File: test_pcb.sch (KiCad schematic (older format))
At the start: 25 parts, among them J1 Conn_01x04_Male, J11 Conn_01x20_Female, J8 Conn_01x20_Female, SW1 on/off, SW2 on/off

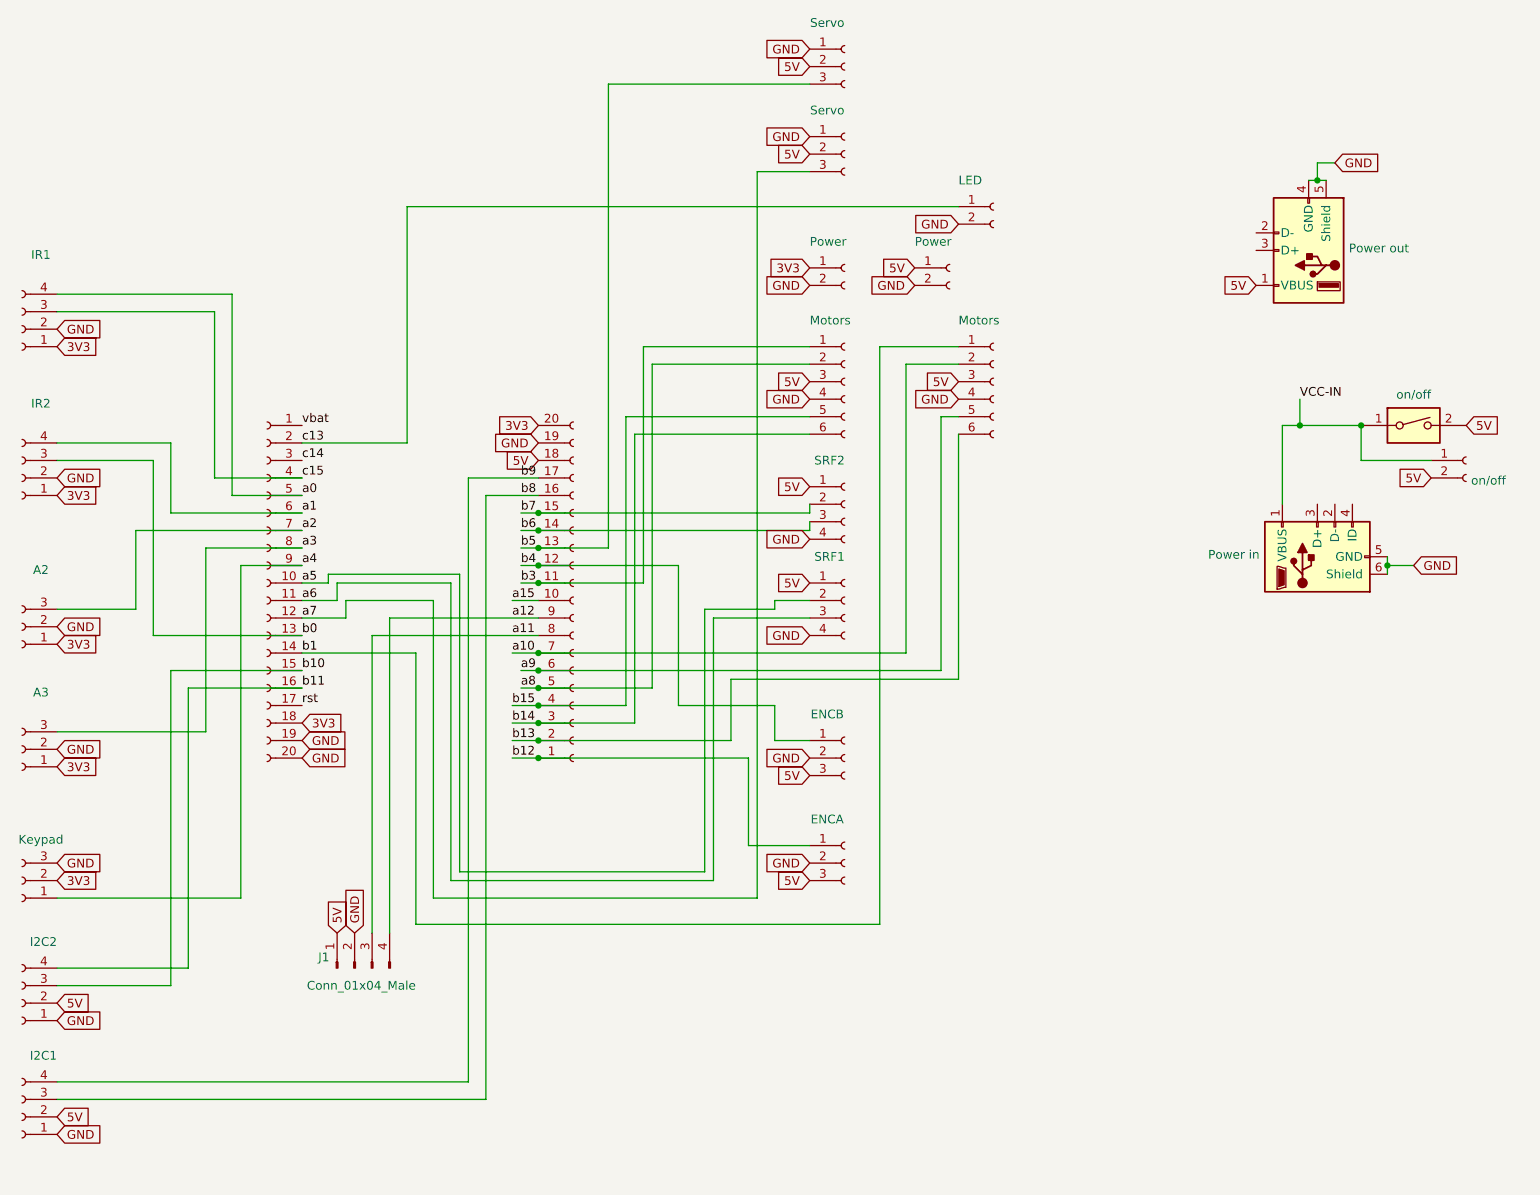
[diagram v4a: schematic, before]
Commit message: routing and shaping, added bom draft
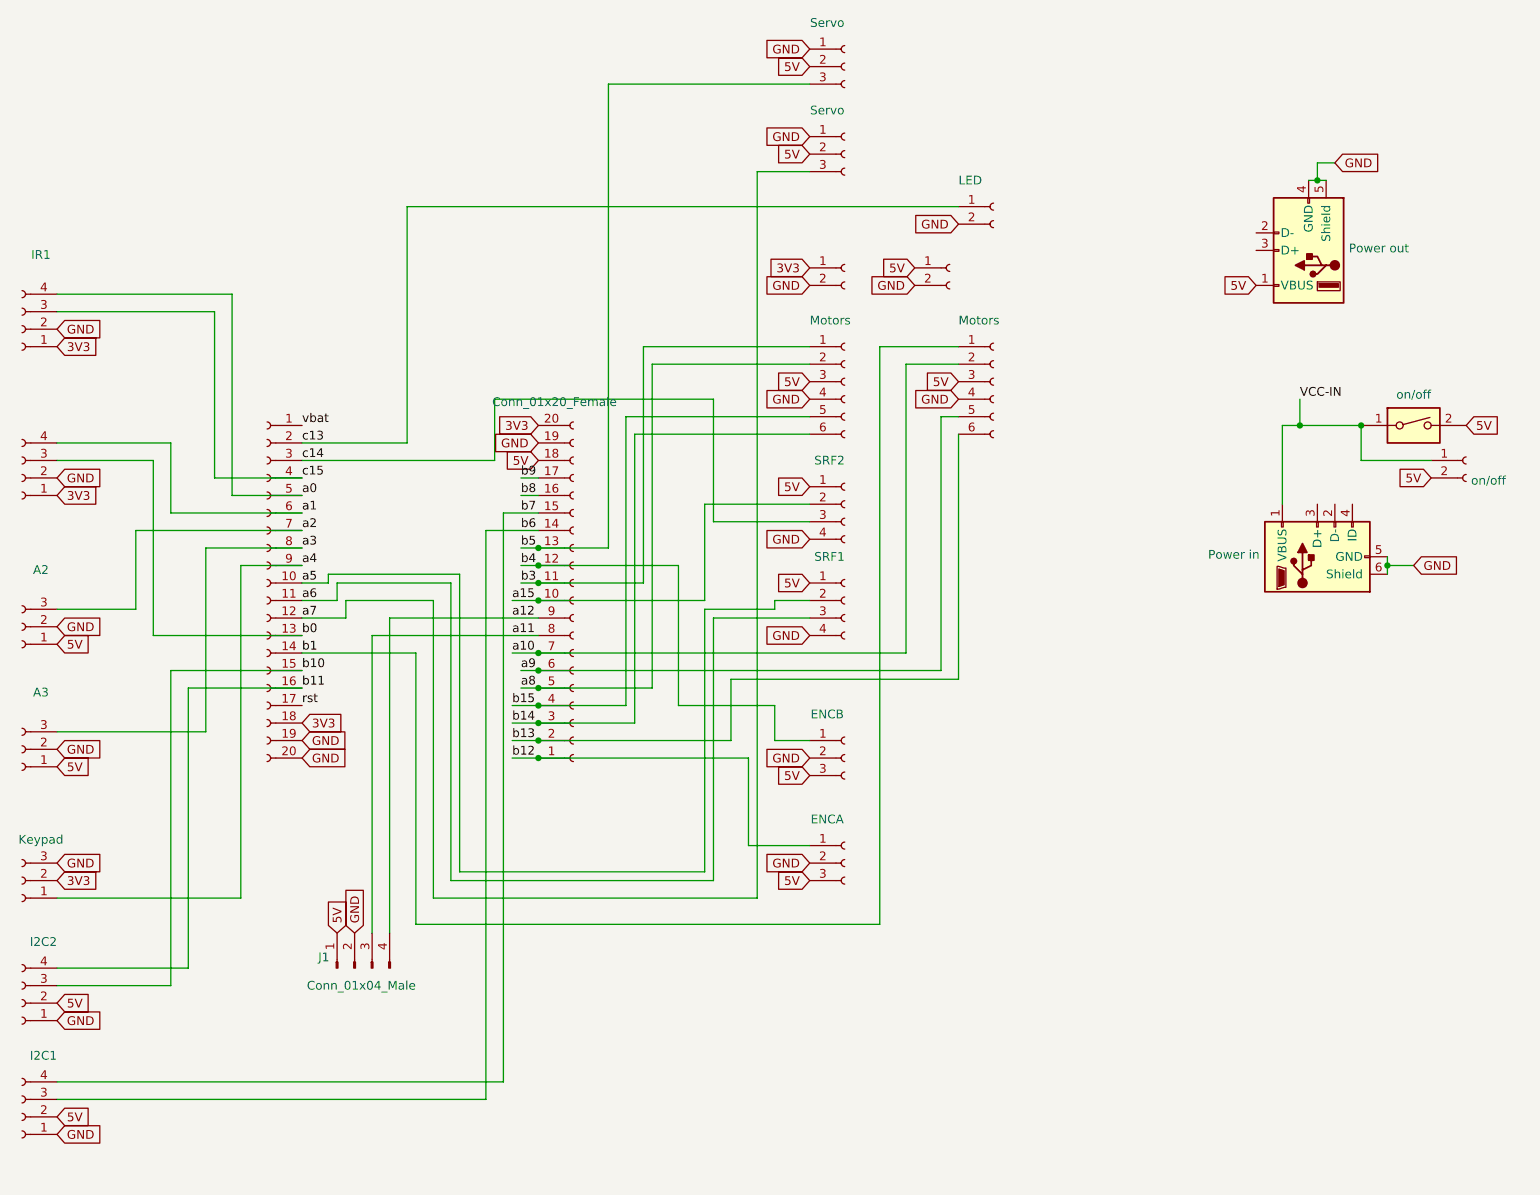
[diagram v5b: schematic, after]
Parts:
- A2: value (A2 GND 3V3) -> A2
- A3: value (A3 GND 3V3) -> A3
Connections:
- net 3V3: no longer A2.1 (Pin_1), A3.1 (Pin_1)
- net 5V: now also A2.1 (Pin_1), A3.1 (Pin_1)
- net a15: now also SRF2.2 (Pin_2)
- net b6: now also I2C1.3 (Pin_3); no longer SRF2.3 (Pin_3)
- net b7: now also I2C1.4 (Pin_4); no longer SRF2.2 (Pin_2)
- net b8: no longer I2C1.3 (Pin_3)
- net b9: no longer I2C1.4 (Pin_4)
- net c14: now also SRF2.3 (Pin_3)
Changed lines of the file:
@@
 P 4100 4300
 F 0 "J11" H 3992 3075 50  0001 C CNN
-F 1 "Conn_01x20_Female" H 3992 3166 50  0001 C CNN
+F 1 "Conn_01x20_Female" H 3992 3166 50  0000 C CNN
 F 2 "Connector_PinSocket_2.54mm:PinSocket_1x20_P2.54mm_Vertical" H 4100 4300 50  0001 C CNN
 F 3 "~" H 4100 4300 50  0001 C CNN
@@
 $EndComp
 $Comp
-L Connector:Conn_01x03_Female A3
-U 1 1 5F73020F
-P 950 5150
-F 0 "A3" H 842 4825 50  0000 C CNN
-F 1 "(A3 GND 3V3)" H 842 4916 50  0001 C CNN
-F 2 "Connector_JST:JST_XH_B3B-XH-A_1x03_P2.50mm_Vertical" H 950 5150 50  0001 C CNN
-F 3 "~" H 950 5150 50  0001 C CNN
-	1    950  5150
-	-1   0    0    1
-$EndComp
-$Comp
-L Connector:Conn_01x03_Female A2
-U 1 1 5F730755
-P 950 4450
-F 0 "A2" H 842 4125 50  0000 C CNN
-F 1 "(A2 GND 3V3)" H 842 4216 50  0001 C CNN
-F 2 "Connector_JST:JST_XH_B3B-XH-A_1x03_P2.50mm_Vertical" H 950 4450 50  0001 C CNN
-F 3 "~" H 950 4450 50  0001 C CNN
-	1    950  4450
-	-1   0    0    1
-$EndComp
-$Comp
 L Connector:Conn_01x04_Female IR2
 U 1 1 5F730AC4
 P 950 3600
-F 0 "IR2" H 842 3175 50  0000 C CNN
+F 0 "IR2" H 842 3175 50  0001 C CNN
 F 1 "(A1 C14 GND 3V3)" H 842 3266 50  0001 C CNN
 F 2 "Connector_JST:JST_XH_B4B-XH-A_1x04_P2.50mm_Vertical" H 950 3600 50  0001 C CNN
@@
 P 5650 2400
 F 0 "Power1" H 5678 2376 50  0001 L CNN
-F 1 "Power" H 5450 2550 50  0000 L CNN
+F 1 "Power" H 5450 2550 50  0001 L CNN
 F 2 "Connector_PinSocket_2.54mm:PinSocket_1x02_P2.54mm_Vertical" H 5650 2400 50  0001 C CNN
 F 3 "~" H 5650 2400 50  0001 C CNN
@@
 	1150 6500 1800 6500
 Wire Wire Line
-	3500 7050 1150 7050
-Wire Wire Line
 	3600 7150 1150 7150
 Wire Wire Line
@@
 	8350 1900 8300 1900
 Text GLabel 1150 5900 2    50   Input ~ 0
-3V3
-Text GLabel 1150 5250 2    50   Input ~ 0
-3V3
-Text GLabel 1150 4550 2    50   Input ~ 0
 3V3
 Text GLabel 1150 3700 2    50   Input ~ 0
@@
 Wire Wire Line
 	2950 6200 2950 4500
-Wire Wire Line
-	2950 4500 3900 4500
-Wire Wire Line
-	3050 4400 3900 4400
 Text GLabel 8000 2500 0    50   Input ~ 0
 5V
@@
 P 6250 2400
 F 0 "Power3" H 6278 2376 50  0001 L CNN
-F 1 "Power" H 6050 2550 50  0000 L CNN
+F 1 "Power" H 6050 2550 50  0001 L CNN
 F 2 "Connector_PinSocket_2.54mm:PinSocket_1x02_P2.54mm_Vertical" H 6250 2400 50  0001 C CNN
 F 3 "~" H 6250 2400 50  0001 C CNN
@@
 3V3
 Wire Wire Line
-	3500 3600 3900 3600
-Wire Wire Line
-	3600 3700 3900 3700
-Wire Wire Line
-	3500 3600 3500 7050
-Wire Wire Line
-	3600 3700 3600 7150
-Wire Wire Line
-	5450 3800 5450 3750
-Wire Wire Line
-	5450 3900 5450 3850
-Wire Wire Line
-	3800 3900 3900 3900
-Connection ~ 3900 3900
-Wire Wire Line
-	3900 3900 5450 3900
-Wire Wire Line
-	3800 3800 3900 3800
-Connection ~ 3900 3800
-Wire Wire Line
-	3900 3800 5450 3800
+	2550 3500 3650 3500
+Wire Wire Line
+	3650 3500 3650 3150
+Wire Wire Line
+	3650 3150 4900 3150
+Wire Wire Line
+	4900 3150 4900 3850
+Wire Wire Line
+	4900 3850 5450 3850
+Wire Wire Line
+	2950 4500 3900 4500
+Wire Wire Line
+	3050 4400 3900 4400
+Wire Wire Line
+	3700 3800 3700 7050
+Wire Wire Line
+	3700 7050 1150 7050
+Wire Wire Line
+	3700 3800 3900 3800
+Wire Wire Line
+	3600 3900 3600 7150
+Wire Wire Line
+	3600 3900 3900 3900
+Wire Wire Line
+	5450 3750 4850 3750
+Wire Wire Line
+	4850 3750 4850 4300
+Wire Wire Line
+	4850 4300 3900 4300
+Connection ~ 3900 4300
+Wire Wire Line
+	3800 3600 3900 3600
+Wire Wire Line
+	3800 3700 3900 3700
+$Comp
+L Connector:Conn_01x03_Female A3
+U 1 1 5F73020F
+P 950 5150
+F 0 "A3" H 842 4825 50  0000 C CNN
+F 1 "A3" H 842 4916 50  0001 C CNN
+F 2 "Connector_JST:JST_XH_B3B-XH-A_1x03_P2.50mm_Vertical" H 950 5150 50  0001 C CNN
+F 3 "~" H 950 5150 50  0001 C CNN
+	1    950  5150
+	-1   0    0    1
+$EndComp
+$Comp
+L Connector:Conn_01x03_Female A2
+U 1 1 5F730755
+P 950 4450
+F 0 "A2" H 842 4125 50  0000 C CNN
+F 1 "A2" H 842 4216 50  0001 C CNN
+F 2 "Connector_JST:JST_XH_B3B-XH-A_1x03_P2.50mm_Vertical" H 950 4450 50  0001 C CNN
+F 3 "~" H 950 4450 50  0001 C CNN
+	1    950  4450
+	-1   0    0    1
+$EndComp
+Text GLabel 1150 5250 2    50   Input ~ 0
+5V
+Text GLabel 1150 4550 2    50   Input ~ 0
+5V
 $EndSCHEMATC

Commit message: fabrication requirements
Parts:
- J14: renamed from SRF2; value (GND A10 B9 5V) -> SRF2
- J15: renamed from SRF1; value (GND A9 B8 5V) -> SRF1
- J16: renamed from IR1; value (A0 C13 GND 3V3) -> IR1
- J17: renamed from IR2; value (A1 C14 GND 3V3) -> IR2
- J18: renamed from I2C2; value (B11 B10 GND 5V) -> I2C2
- J19: renamed from I2C1; value (B7 B6 GND 5V) -> I2C1
- J6: renamed from Servo1; value Servo -> Servo1
- J7: renamed from Servo2; value Servo -> Servo2
- J9: renamed from mc2; value Motors -> MC2
- renumbered J8 to J10, Power_out1 to J12, Power_in1 to J13, SW2 to J2, A2 to J20, A3 to J21, Keys1 to J22, ENCB1 to J23, ENCA1 to J24, Power2 to J3, Power1 to J4, Power3 to J5, mc1 to J8

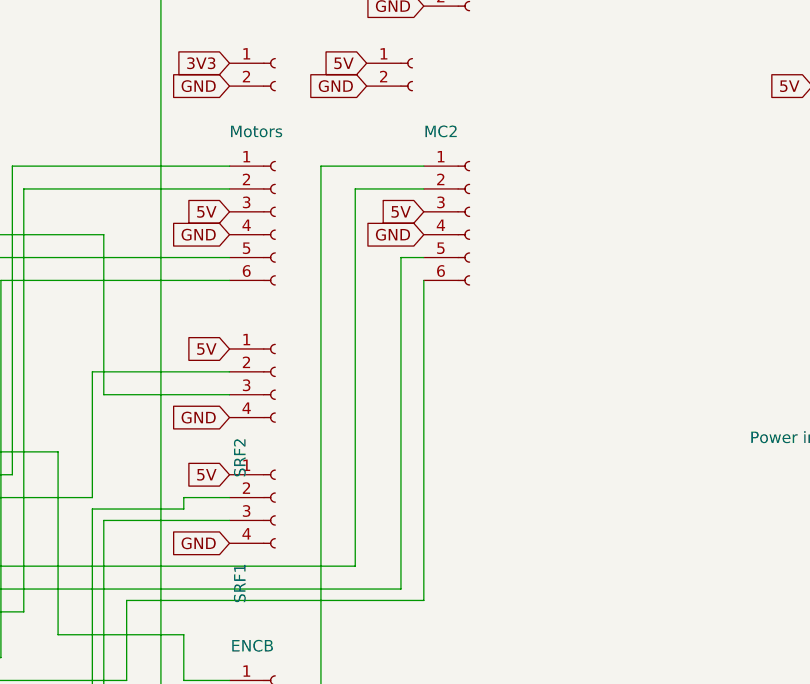
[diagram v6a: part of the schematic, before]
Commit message: removed gerber files
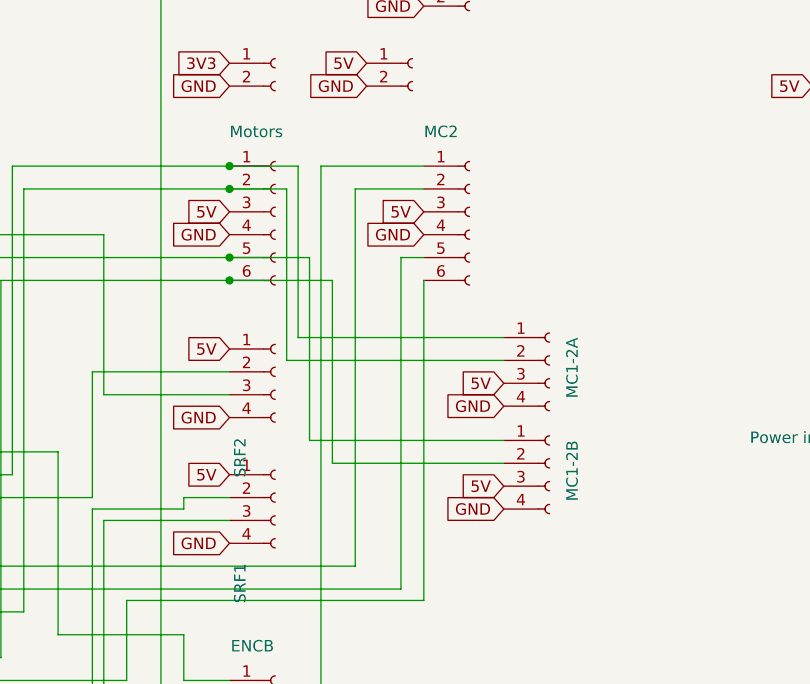
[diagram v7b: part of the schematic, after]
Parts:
- added J25: MC1-2A, Connector_JST:JST_XH_B4B-XH-A_1x04_P2.50mm_Vertical, symbol Connector:Conn_01x04_Female
- added J26: MC1-2B, Connector_JST:JST_XH_B4B-XH-A_1x04_P2.50mm_Vertical, symbol Connector:Conn_01x04_Female
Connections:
- net 5V: now also J25.3 (Pin_3), J26.3 (Pin_3)
- net GND: now also J25.4 (Pin_4), J26.4 (Pin_4)
- net a8: now also J25.2 (Pin_2)
- net b14: now also J26.2 (Pin_2)
- net b15: now also J26.1 (Pin_1)
- net b3: now also J25.1 (Pin_1)
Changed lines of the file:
@@
 	3200 6150 5850 6150
-Wire Wire Line
-	5850 6150 5850 2850
 Wire Wire Line
 	5850 2850 6300 2850
@@
 	-1   0    0    1
 $EndComp
+$Comp
+L Connector:Conn_01x04_Female J25
+U 1 1 604624D0
+P 6850 3700
+F 0 "J25" H 6850 3950 50  0001 R CNN
+F 1 "MC1-2A" V 6950 3800 50  0000 R CNN
+F 2 "Connector_JST:JST_XH_B4B-XH-A_1x04_P2.50mm_Vertical" H 6850 3700 50  0001 C CNN
+F 3 "~" H 6850 3700 50  0001 C CNN
+	1    6850 3700
+	1    0    0    -1
+$EndComp
+$Comp
+L Connector:Conn_01x04_Female J26
+U 1 1 60462CE1
+P 6850 4150
+F 0 "J26" H 6850 4400 50  0001 R CNN
+F 1 "MC1-2B" V 6950 4250 50  0000 R CNN
+F 2 "Connector_JST:JST_XH_B4B-XH-A_1x04_P2.50mm_Vertical" H 6850 4150 50  0001 C CNN
+F 3 "~" H 6850 4150 50  0001 C CNN
+	1    6850 4150
+	1    0    0    -1
+$EndComp
+Wire Wire Line
+	5450 2850 5750 2850
+Wire Wire Line
+	5750 2850 5750 3600
+Wire Wire Line
+	5750 3600 6650 3600
+Connection ~ 5450 2850
+Wire Wire Line
+	5450 2950 5700 2950
+Wire Wire Line
+	5700 2950 5700 3700
+Wire Wire Line
+	5700 3700 6650 3700
+Connection ~ 5450 2950
+Wire Wire Line
+	5850 6150 5850 2850
+Wire Wire Line
+	5450 3250 5800 3250
+Wire Wire Line
+	5800 3250 5800 4050
+Wire Wire Line
+	5800 4050 6650 4050
+Connection ~ 5450 3250
+Wire Wire Line
+	5450 3350 5900 3350
+Wire Wire Line
+	5900 3350 5900 4150
+Wire Wire Line
+	5900 4150 6650 4150
+Connection ~ 5450 3350
+Text GLabel 6650 3800 0    50   Input ~ 0
+5V
+Text GLabel 6650 4250 0    50   Input ~ 0
+5V
+Text GLabel 6650 3900 0    50   Input ~ 0
+GND
+Text GLabel 6650 4350 0    50   Input ~ 0
+GND
 $EndSCHEMATC
